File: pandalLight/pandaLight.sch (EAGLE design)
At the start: 114 parts, among them J1 PJ-037A, U13 TPD12S016PWR, U15 PMOD-2X6, U16 PMOD-2X6, U17 PLR135-T10, U18 PLT133-T10W, U20 TP10SQ, U21 TP10SQ, U22 PAN1322, U23 6SLX9TQG144, U4 FT2232HL, U5 93LC46BT-I/OT, U6 51, U7 51, U8 TPD12S016PWR, X1 USBUB-S, X2 HDMI_RECEPTICAL_A, X4 HDMI_RECEPTICAL_A, Y1 403, Y2 20Mhz

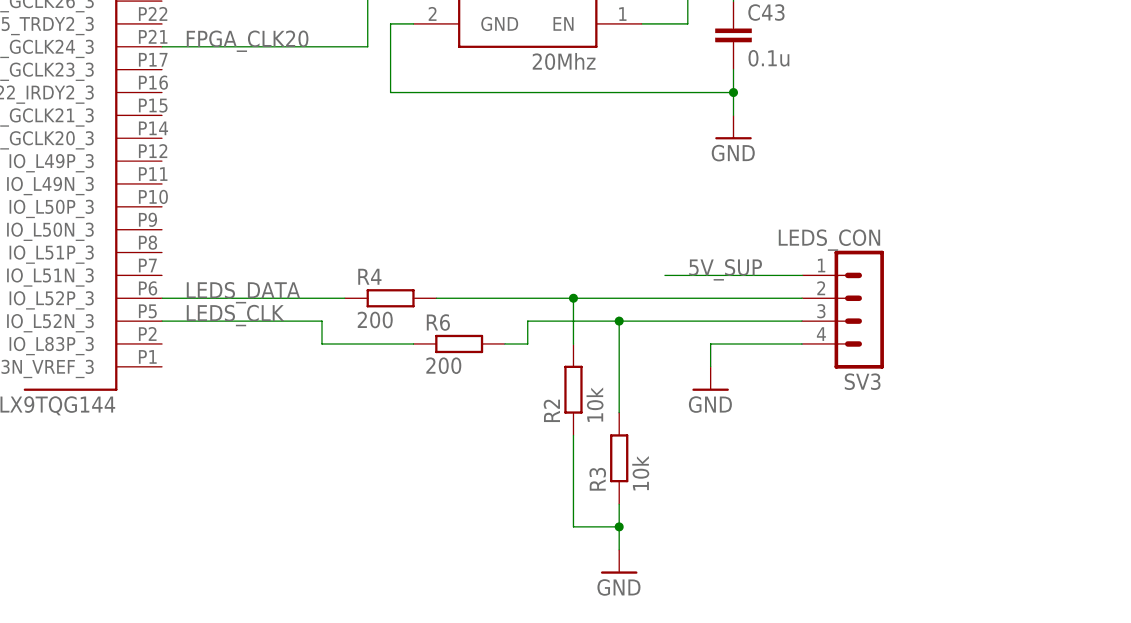
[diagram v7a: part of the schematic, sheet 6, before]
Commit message: Added LED signal CMOS to TTL level shifter
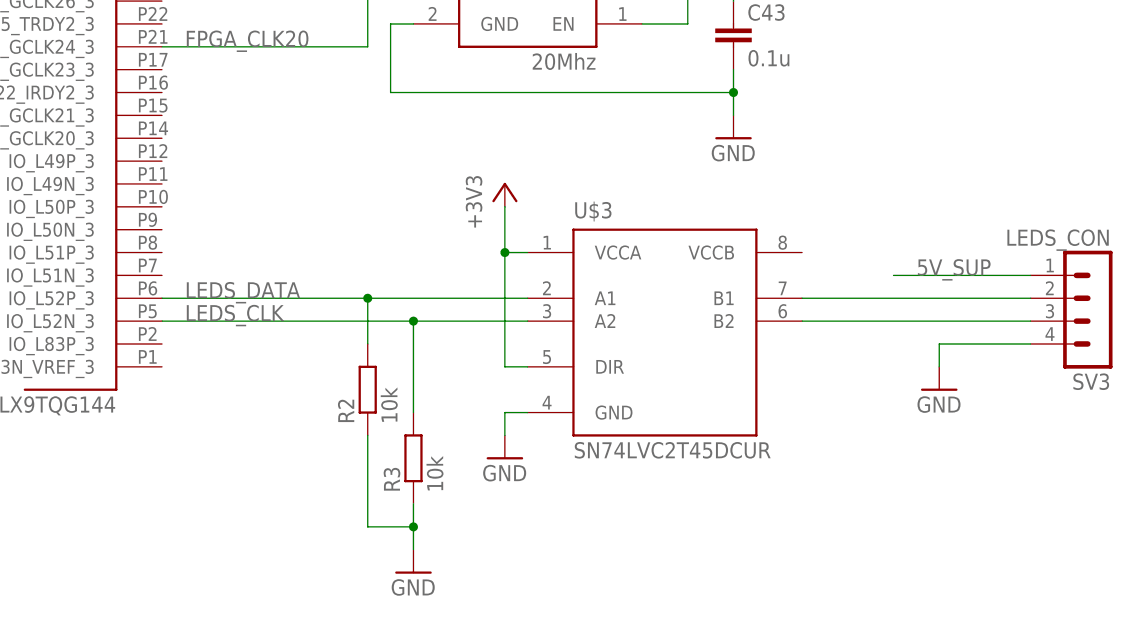
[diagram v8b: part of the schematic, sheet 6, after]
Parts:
- removed R4, R6: 200, pandaLight:RESISTOR0402
- added U$3: SN74LVC2T45DCUR, pandaLight:SN74LVC2T45DCUR
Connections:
- net +3V3: now also U$3.DIR, U$3.VCCA
- net GND: now also U$3.GND
- net LEDS_CLK: now also R3.2, U$3.A2; no longer R6.1
- net LEDS_DATA: now also R2.2, U$3.A1; no longer R4.1
- net N$2: now also U$3.B1; no longer R2.2, R4.2
- net N$3: now also U$3.B2; no longer R3.2, R6.2
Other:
- moved on the sheet: R2, R3, SV3
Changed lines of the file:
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@@
 <part name="R3" library="pandaLight" deviceset="RESISTOR" device="0402" value="10k"/>
 <part name="GND16" library="pandaLight" deviceset="GND" device=""/>
-<part name="R4" library="pandaLight" deviceset="RESISTOR" device="0402" value="200"/>
-<part name="R6" library="pandaLight" deviceset="RESISTOR" device="0402" value="200"/>
+<part name="U$3" library="pandaLight" deviceset="SN74LVC2T45" device="DCUR"/>
+<part name="PS3" library="pandaLight" deviceset="+3V3" device=""/>
+<part name="GND17" library="pandaLight" deviceset="GND" device=""/>
 </parts>
 <sheets>
@@
 <instance part="GND46" gate="1" x="66.04" y="81.28"/>
 <instance part="U23" gate="B3" x="30.48" y="48.26"/>
-<instance part="SV3" gate="G$1" x="114.3" y="17.78" rot="R180">
-<attribute name="PARTNO" x="114.3" y="17.78" size="1.778" layer="96" display="off"/>
-<attribute name="BOM" x="114.3" y="17.78" size="1.778" layer="96" rot="R180" display="off"/>
+<instance part="SV3" gate="G$1" x="139.7" y="17.78" rot="R180">
+<attribute name="PARTNO" x="139.7" y="17.78" size="1.778" layer="96" display="off"/>
+<attribute name="BOM" x="139.7" y="17.78" size="1.778" layer="96" rot="R180" display="off"/>
 </instance>
 <instance part="Y2" gate="G$1" x="76.2" y="53.34" rot="MR0">
@@
 </instance>
 <instance part="GND32" gate="1" x="99.06" y="38.1"/>
-<instance part="GND7" gate="1" x="96.52" y="10.16"/>
-<instance part="R2" gate="G$1" x="81.28" y="10.16" rot="R90"/>
-<instance part="R3" gate="G$1" x="86.36" y="2.54" rot="R90"/>
-<instance part="GND16" gate="1" x="86.36" y="-10.16"/>
-<instance part="R4" gate="G$1" x="60.96" y="20.32"/>
-<instance part="R6" gate="G$1" x="68.58" y="15.24"/>
+<instance part="GND7" gate="1" x="121.92" y="10.16"/>
+<instance part="R2" gate="G$1" x="58.42" y="10.16" rot="R90"/>
+<instance part="R3" gate="G$1" x="63.5" y="2.54" rot="R90"/>
+<instance part="GND16" gate="1" x="63.5" y="-10.16"/>
+<instance part="U$3" gate="G$1" x="91.44" y="17.78"/>
+<instance part="PS3" gate="G$1" x="73.66" y="33.02"/>
+<instance part="GND17" gate="1" x="73.66" y="2.54"/>
 </instances>
 <busses>
@@
 <segment>
 <pinref part="SV3" gate="G$1" pin="4"/>
-<wire x1="106.68" y1="15.24" x2="96.52" y2="15.24" width="0.1524" layer="91"/>
-<wire x1="96.52" y1="15.24" x2="96.52" y2="12.7" width="0.1524" layer="91"/>
+<wire x1="132.08" y1="15.24" x2="121.92" y2="15.24" width="0.1524" layer="91"/>
+<wire x1="121.92" y1="15.24" x2="121.92" y2="12.7" width="0.1524" layer="91"/>
 <pinref part="GND7" gate="1" pin="GND"/>
 </segment>
 <segment>
 <pinref part="R2" gate="G$1" pin="1"/>
-<wire x1="81.28" y1="5.08" x2="81.28" y2="-5.08" width="0.1524" layer="91"/>
+<wire x1="58.42" y1="5.08" x2="58.42" y2="-5.08" width="0.1524" layer="91"/>
 <pinref part="R3" gate="G$1" pin="1"/>
-<wire x1="81.28" y1="-5.08" x2="86.36" y2="-5.08" width="0.1524" layer="91"/>
-<wire x1="86.36" y1="-5.08" x2="86.36" y2="-2.54" width="0.1524" layer="91"/>
+<wire x1="58.42" y1="-5.08" x2="63.5" y2="-5.08" width="0.1524" layer="91"/>
+<wire x1="63.5" y1="-5.08" x2="63.5" y2="-2.54" width="0.1524" layer="91"/>
 <pinref part="GND16" gate="1" pin="GND"/>
-<wire x1="86.36" y1="-5.08" x2="86.36" y2="-7.62" width="0.1524" layer="91"/>
-<junction x="86.36" y="-5.08"/>
+<wire x1="63.5" y1="-5.08" x2="63.5" y2="-7.62" width="0.1524" layer="91"/>
+<junction x="63.5" y="-5.08"/>
+</segment>
+<segment>
+<pinref part="U$3" gate="G$1" pin="GND"/>
+<pinref part="GND17" gate="1" pin="GND"/>
+<wire x1="76.2" y1="7.62" x2="73.66" y2="7.62" width="0.1524" layer="91"/>
+<wire x1="73.66" y1="7.62" x2="73.66" y2="5.08" width="0.1524" layer="91"/>
 </segment>
 </net>
@@
 <segment>
 <pinref part="U23" gate="B3" pin="IO_L52P_3"/>
-<wire x1="35.56" y1="20.32" x2="55.88" y2="20.32" width="0.1524" layer="91"/>
+<wire x1="35.56" y1="20.32" x2="58.42" y2="20.32" width="0.1524" layer="91"/>
 <label x="38.1" y="20.32" size="1.778" layer="95"/>
-<pinref part="R4" gate="G$1" pin="1"/>
+<pinref part="R2" gate="G$1" pin="2"/>
+<wire x1="58.42" y1="15.24" x2="58.42" y2="20.32" width="0.1524" layer="91"/>
+<pinref part="U$3" gate="G$1" pin="A1"/>
+<wire x1="58.42" y1="20.32" x2="76.2" y2="20.32" width="0.1524" layer="91"/>
+<junction x="58.42" y="20.32"/>
 </segment>
 </net>
@@
 <pinref part="U23" gate="B3" pin="IO_L52N_3"/>
 <label x="38.1" y="17.78" size="1.778" layer="95"/>
-<wire x1="53.34" y1="17.78" x2="35.56" y2="17.78" width="0.1524" layer="91"/>
-<wire x1="53.34" y1="17.78" x2="53.34" y2="15.24" width="0.1524" layer="91"/>
-<pinref part="R6" gate="G$1" pin="1"/>
-<wire x1="53.34" y1="15.24" x2="63.5" y2="15.24" width="0.1524" layer="91"/>
+<pinref part="R3" gate="G$1" pin="2"/>
+<wire x1="63.5" y1="17.78" x2="63.5" y2="7.62" width="0.1524" layer="91"/>
+<wire x1="35.56" y1="17.78" x2="63.5" y2="17.78" width="0.1524" layer="91"/>
+<pinref part="U$3" gate="G$1" pin="A2"/>
+<wire x1="63.5" y1="17.78" x2="76.2" y2="17.78" width="0.1524" layer="91"/>
+<junction x="63.5" y="17.78"/>
 </segment>
 </net>
@@
 <wire x1="99.06" y1="55.88" x2="99.06" y2="53.34" width="0.1524" layer="91"/>
 </segment>
+<segment>
+<pinref part="U$3" gate="G$1" pin="VCCA"/>
+<pinref part="PS3" gate="G$1" pin="+3V3"/>
+<wire x1="76.2" y1="25.4" x2="73.66" y2="25.4" width="0.1524" layer="91"/>
+<wire x1="73.66" y1="25.4" x2="73.66" y2="30.48" width="0.1524" layer="91"/>
+<pinref part="U$3" gate="G$1" pin="DIR"/>
+<wire x1="76.2" y1="12.7" x2="73.66" y2="12.7" width="0.1524" layer="91"/>
+<wire x1="73.66" y1="12.7" x2="73.66" y2="25.4" width="0.1524" layer="91"/>
+<junction x="73.66" y="25.4"/>
+</segment>
 </net>
 <net name="FPGA_CLK20" class="0">
@@
 <segment>
 <pinref part="SV3" gate="G$1" pin="1"/>
-<wire x1="106.68" y1="22.86" x2="91.44" y2="22.86" width="0.1524" layer="91"/>
-<label x="93.98" y="22.86" size="1.778" layer="95"/>
+<wire x1="132.08" y1="22.86" x2="116.84" y2="22.86" width="0.1524" layer="91"/>
+<label x="119.38" y="22.86" size="1.778" layer="95"/>
 </segment>
 </net>
 <net name="N$2" class="0">
 <segment>
-<pinref part="R4" gate="G$1" pin="2"/>
+<pinref part="U$3" gate="G$1" pin="B1"/>
 <pinref part="SV3" gate="G$1" pin="2"/>
-<wire x1="66.04" y1="20.32" x2="81.28" y2="20.32" width="0.1524" layer="91"/>
-<pinref part="R2" gate="G$1" pin="2"/>
-<wire x1="81.28" y1="20.32" x2="106.68" y2="20.32" width="0.1524" layer="91"/>
-<wire x1="81.28" y1="15.24" x2="81.28" y2="20.32" width="0.1524" layer="91"/>
-<junction x="81.28" y="20.32"/>
+<wire x1="106.68" y1="20.32" x2="132.08" y2="20.32" width="0.1524" layer="91"/>
 </segment>
 </net>
@@
 <segment>
 <pinref part="SV3" gate="G$1" pin="3"/>
-<wire x1="106.68" y1="17.78" x2="86.36" y2="17.78" width="0.1524" layer="91"/>
-<wire x1="86.36" y1="17.78" x2="76.2" y2="17.78" width="0.1524" layer="91"/>
-<wire x1="76.2" y1="17.78" x2="76.2" y2="15.24" width="0.1524" layer="91"/>
-<pinref part="R6" gate="G$1" pin="2"/>
-<wire x1="76.2" y1="15.24" x2="73.66" y2="15.24" width="0.1524" layer="91"/>
-<pinref part="R3" gate="G$1" pin="2"/>
-<wire x1="86.36" y1="17.78" x2="86.36" y2="7.62" width="0.1524" layer="91"/>
-<junction x="86.36" y="17.78"/>
-</segment>
-</net>
+<pinref part="U$3" gate="G$1" pin="B2"/>
+<wire x1="132.08" y1="17.78" x2="106.68" y2="17.78" width="0.1524" layer="91"/>
+</segment>
+</net>
